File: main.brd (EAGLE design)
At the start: 50.8 x 50.8 mm, 54 parts, among them U2 SN65HVD32_D_8

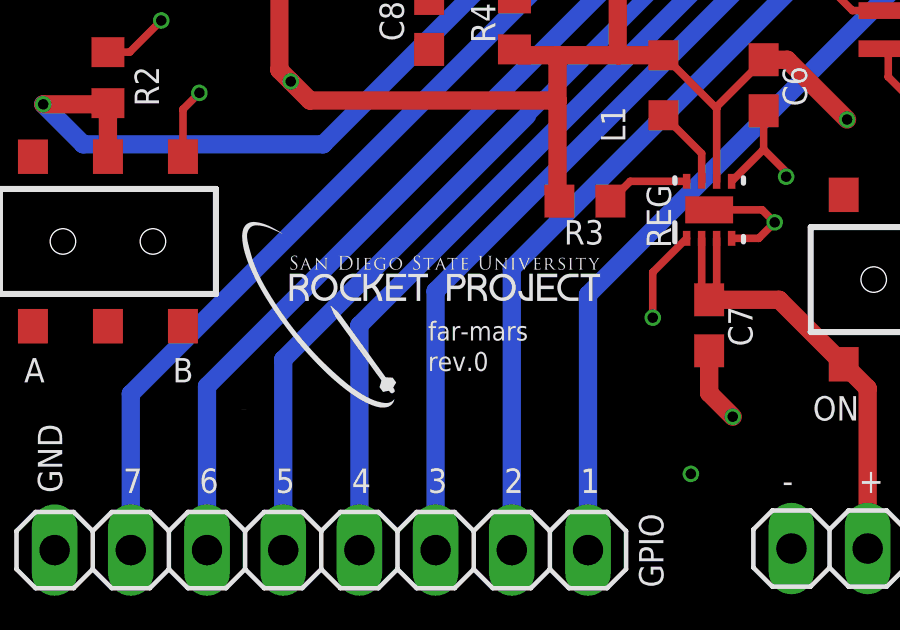
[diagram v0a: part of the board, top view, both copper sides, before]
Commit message: Some logo dpi fixes
OSHpark wouldn't except a silkscreen above 400 dpi
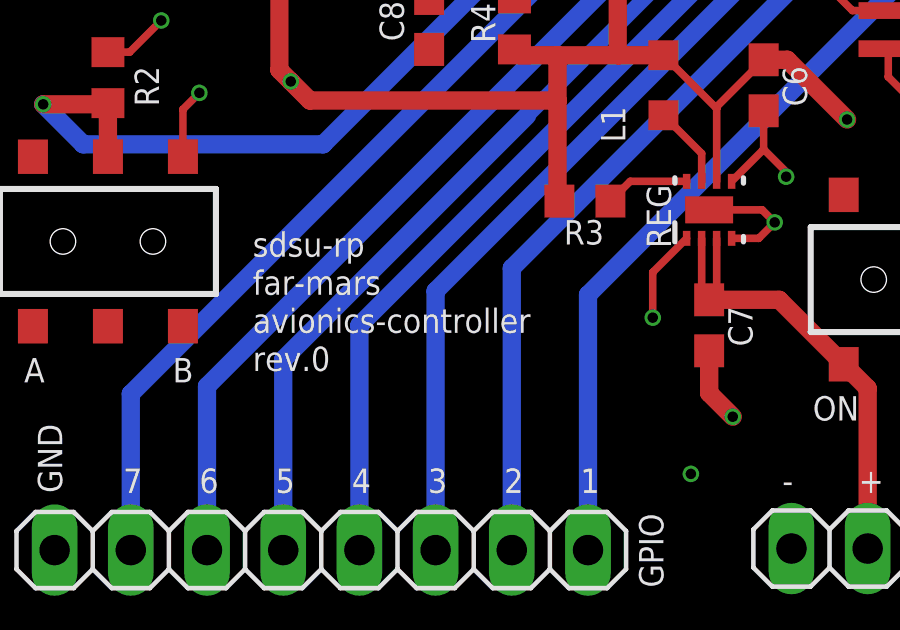
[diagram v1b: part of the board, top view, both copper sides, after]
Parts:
- removed U$6: (no value), cool:RP-LOGO-.15
- added U$5: (no value), cool:RP-LOGO-DPIFIX
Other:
- board text added: "avionics-controller"
- board text added: "sdsu-rp"
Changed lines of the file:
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@@
 <layers>
 <layer number="1" name="Top" color="4" fill="1" visible="yes" active="yes"/>
-<layer number="2" name="Route2" color="1" fill="3" visible="yes" active="yes"/>
+<layer number="2" name="Route2" color="1" fill="3" visible="no" active="yes"/>
 <layer number="3" name="Route3" color="4" fill="3" visible="no" active="no"/>
 <layer number="4" name="Route4" color="1" fill="4" visible="no" active="no"/>
@@
 <layer number="13" name="Route13" color="4" fill="5" visible="no" active="no"/>
 <layer number="14" name="Route14" color="1" fill="6" visible="no" active="no"/>
-<layer number="15" name="Route15" color="4" fill="6" visible="yes" active="yes"/>
-<layer number="16" name="Bottom" color="1" fill="1" visible="yes" active="yes"/>
+<layer number="15" name="Route15" color="4" fill="6" visible="no" active="yes"/>
+<layer number="16" name="Bottom" color="1" fill="1" visible="no" active="yes"/>
 <layer number="17" name="Pads" color="2" fill="1" visible="yes" active="yes"/>
 <layer number="18" name="Vias" color="2" fill="1" visible="yes" active="yes"/>
@@
 <text x="10.414" y="8.89" size="0.8128" layer="25">A</text>
 <text x="15.367" y="8.89" size="0.8128" layer="25">B</text>
-<text x="23.876" y="10.287" size="0.635" layer="21" font="vector">far-mars</text>
-<text x="23.876" y="9.271" size="0.635" layer="21" font="vector">rev.0</text>
+<text x="18.034" y="11.811" size="0.8128" layer="21" font="vector">far-mars</text>
+<text x="18.034" y="9.271" size="0.8128" layer="21" font="vector">rev.0</text>
+<text x="18.034" y="13.081" size="0.8128" layer="21" font="vector">sdsu-rp</text>
+<text x="18.034" y="10.541" size="0.8128" layer="21" font="vector">avionics-controller</text>
 </plain>
 <attributes>
@@
 <attribute name="VALUE" x="11.303" y="19.685" size="1.27" layer="27" rot="R270"/>
 </element>
-<element name="U$6" library="cool" package="RP-LOGO-.15" value="" x="17.653" y="8.001"/>
+<element name="U$5" library="cool" package="RP-LOGO-DPIFIX" value="" x="43.688" y="11.811" rot="MR0"/>
 </elements>
 <signals>

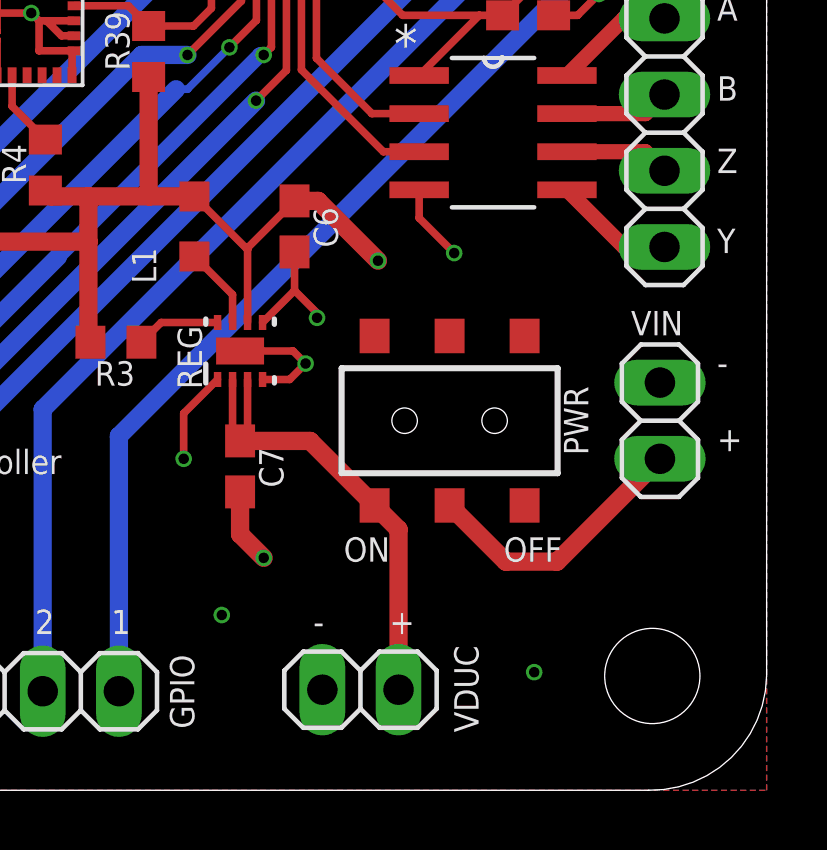
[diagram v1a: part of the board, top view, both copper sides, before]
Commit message: Small switch adjustment, and render update for this change
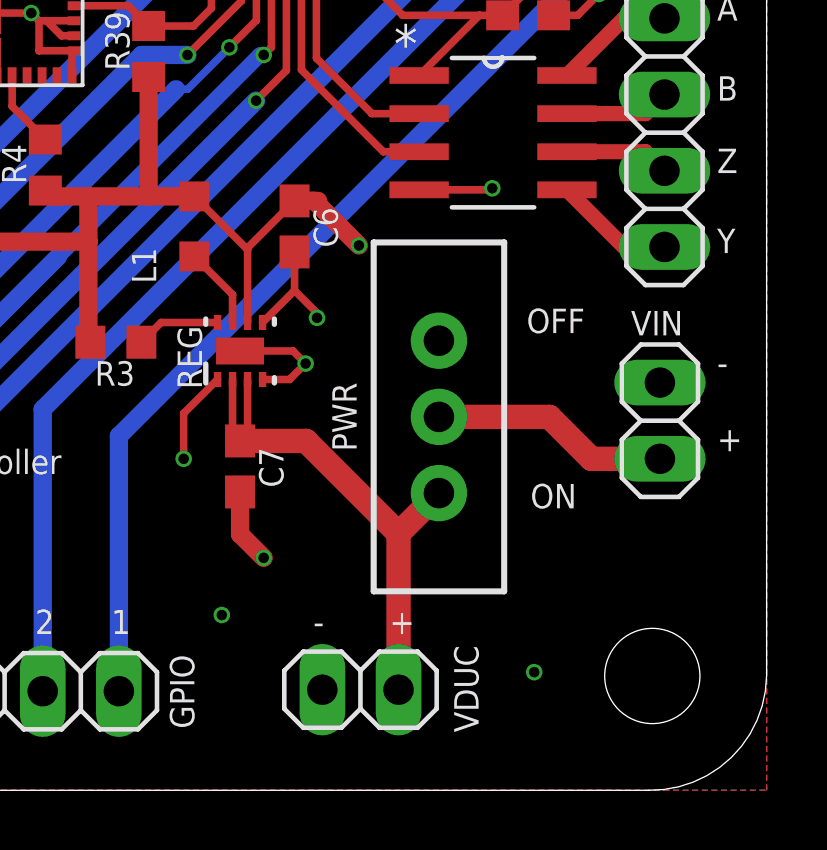
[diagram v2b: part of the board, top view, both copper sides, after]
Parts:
- PWR: device SparkFun-Switches:SWITCH_DPDT_SMD_AYZ0202 -> SparkFun-Switches:SWITCH_SPDT_PTH_11.6X4.0MM
- moved PWR 0.38 mm to (39.9, 12.4)
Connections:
- net VSYS: now also PWR.1; no longer PWR.3
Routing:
- net VSYS: track 16.2 -> 18.0 mm
- net N$9: track 9.21 -> 7.94 mm
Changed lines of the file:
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@@
 <text x="49.149" y="13.843" size="0.8128" layer="25">-</text>
 <text x="49.149" y="11.303" size="0.8128" layer="25">+</text>
-<text x="36.703" y="7.62" size="0.8128" layer="25">ON</text>
-<text x="42.037" y="7.62" size="0.8128" layer="25">OFF</text>
+<text x="42.926" y="9.398" size="0.8128" layer="25">ON</text>
+<text x="42.799" y="15.24" size="0.8128" layer="25">OFF</text>
 <text x="5.334" y="15.494" size="0.8128" layer="25">-</text>
 <text x="5.334" y="12.954" size="0.8128" layer="25">+</text>
@@
 <attribute name="VALUE" x="33.1597" y="19.431" size="1.27" layer="27" rot="R270"/>
 </element>
-<element name="PWR" library="SparkFun-Switches" package="SWITCH_DPDT_SMD_AYZ0202" value="" x="40.2336" y="12.319" smashed="yes" rot="R180">
-<attribute name="NAME" x="44.0436" y="12.319" size="0.8128" layer="25" ratio="20" rot="R270" align="bottom-center"/>
-<attribute name="PROD_ID" value="SWCH-08179" x="49.5808" y="25.1079" size="1.778" layer="27" rot="R180" display="off"/>
-<attribute name="SF_ID" value="COM-00597" x="49.5808" y="25.1079" size="1.778" layer="27" rot="R180" display="off"/>
-<attribute name="VALUE" x="36.4236" y="12.319" size="0.6096" layer="27" font="vector" ratio="20" rot="R270" align="top-center"/>
-</element>
 <element name="C7" library="resistor" package="C0603" value="10u" x="33.2486" y="10.795" smashed="yes" rot="R270">
 <attribute name="NAME" x="33.8836" y="11.43" size="0.8128" layer="25" rot="R270"/>
@@
 </element>
 <element name="U$5" library="cool" package="RP-LOGO-DPIFIX" value="" x="43.688" y="11.811" rot="MR0"/>
+<element name="PWR" library="SparkFun-Switches" package="SWITCH_SPDT_PTH_11.6X4.0MM" value="" x="39.878" y="12.446" smashed="yes" rot="R180">
+<attribute name="NAME" x="36.322" y="12.446" size="0.8128" layer="25" ratio="20" rot="R270" align="bottom-center"/>
+<attribute name="PROD_ID" value="SWCH-08261" x="39.878" y="12.446" size="1.778" layer="27" rot="R180" display="off"/>
+<attribute name="SF_SKU" value="COM-00102" x="39.878" y="12.446" size="1.778" layer="27" rot="R180" display="off"/>
+<attribute name="VALUE" x="37.465" y="12.446" size="0.6096" layer="27" font="vector" ratio="20" rot="R270" align="top-center"/>
+</element>
 </elements>
 <signals>
@@
 <wire x1="28.194" y1="14.9996" x2="28.2584" y2="14.9352" width="0.6096" layer="1"/>
 <wire x1="35.0647" y1="19.646" x2="35.853" y2="19.646" width="0.6096" layer="1"/>
-<wire x1="35.853" y1="19.646" x2="37.846" y2="17.653" width="0.6096" layer="1"/>
-<via x="37.846" y="17.653" extent="1-16" drill="0.35"/>
 <wire x1="28.194" y1="18.288" x2="19.939" y2="18.288" width="0.6096" layer="1"/>
 <wire x1="19.939" y1="18.288" x2="19.304" y2="18.923" width="0.6096" layer="1"/>
@@
 <via x="46.609" y="29.083" extent="1-16" drill="0.35"/>
 <wire x1="48.1457" y1="29.1093" x2="46.6353" y2="29.1093" width="0.254" layer="1"/>
+<wire x1="35.0647" y1="19.646" x2="35.726" y2="19.646" width="0.6096" layer="1"/>
+<wire x1="35.726" y1="19.646" x2="37.211" y2="18.161" width="0.6096" layer="1"/>
+<via x="37.211" y="18.161" extent="1-16" drill="0.35"/>
 </signal>
 <signal name="GND">
@@
 <wire x1="44.5008" y1="25.8318" x2="45.212" y2="26.543" width="0.254" layer="1"/>
 <via x="45.212" y="26.543" extent="1-16" drill="0.35"/>
-<wire x1="39.2176" y1="20.0152" x2="39.2176" y2="19.0754" width="0.254" layer="1"/>
-<wire x1="39.2176" y1="19.0754" x2="40.386" y2="17.907" width="0.254" layer="1"/>
-<via x="40.386" y="17.907" extent="1-16" drill="0.35"/>
 <wire x1="35.0647" y1="16.6592" x2="35.814" y2="15.9099" width="0.254" layer="1"/>
 <wire x1="35.814" y1="15.9099" x2="35.814" y2="15.748" width="0.254" layer="1"/>
@@
 <wire x1="25.15" y1="25.908" x2="26.289" y2="25.908" width="0.254" layer="1"/>
 <contactref element="GPIO" pad="8"/>
+<wire x1="39.2176" y1="20.0152" x2="41.6052" y2="20.0152" width="0.254" layer="1"/>
+<wire x1="41.6052" y1="20.0152" x2="41.656" y2="20.066" width="0.254" layer="1"/>
+<via x="41.656" y="20.066" extent="1-16" drill="0.35"/>
 </signal>
 <signal name="VDDCORE">
@@
 <contactref element="REG" pad="3"/>
 <contactref element="C7" pad="1"/>
-<contactref element="PWR" pad="3"/>
 <wire x1="33.2486" y1="11.645" x2="33.4986" y2="11.895" width="0.254" layer="1"/>
 <wire x1="33.4986" y1="11.895" x2="33.4986" y2="13.6931" width="0.254" layer="1"/>
 <wire x1="32.998596875" y1="13.6931" x2="32.998596875" y2="11.895003125" width="0.254" layer="1"/>
 <wire x1="32.998596875" y1="11.895003125" x2="33.2486" y2="11.645" width="0.254" layer="1"/>
-<wire x1="37.7336" y1="9.494" x2="35.5826" y2="11.645" width="0.6096" layer="1"/>
-<wire x1="35.5826" y1="11.645" x2="33.2486" y2="11.645" width="0.6096" layer="1"/>
-<wire x1="38.5318" y1="3.3528" x2="38.5318" y2="8.6958" width="0.6096" layer="1"/>
-<wire x1="38.5318" y1="8.6958" x2="37.7336" y2="9.494" width="0.6096" layer="1"/>
+<contactref element="PWR" pad="1"/>
+<wire x1="39.878" y1="9.906" x2="38.5318" y2="8.5598" width="0.8128" layer="1"/>
+<wire x1="38.5318" y1="8.5598" x2="38.5318" y2="3.3528" width="0.8128" layer="1"/>
+<wire x1="33.2486" y1="11.645" x2="35.4466" y2="11.645" width="0.8128" layer="1"/>
+<wire x1="35.4466" y1="11.645" x2="38.5318" y2="8.5598" width="0.8128" layer="1"/>
 </signal>
 <signal name="N$8">
@@
 </signal>
 <signal name="N$9">
+<contactref element="VIN" pad="2"/>
 <contactref element="PWR" pad="2"/>
-<contactref element="VIN" pad="2"/>
-<wire x1="40.2336" y1="9.494" x2="42.1076" y2="7.62" width="0.6096" layer="1"/>
-<wire x1="43.815" y1="7.62" x2="47.244" y2="11.049" width="0.6096" layer="1"/>
-<wire x1="42.1076" y1="7.62" x2="43.815" y2="7.62" width="0.6096" layer="1"/>
+<wire x1="47.244" y1="11.049" x2="44.958" y2="11.049" width="0.8128" layer="1"/>
+<wire x1="44.958" y1="11.049" x2="43.561" y2="12.446" width="0.8128" layer="1"/>
+<wire x1="43.561" y1="12.446" x2="39.878" y2="12.446" width="0.8128" layer="1"/>
 </signal>
 <signal name="GPIO1">

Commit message: Layout overview
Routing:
- net GND: track 84.7 -> 80.3 mm, vias 38 -> 41
- net VSYS: track 18.0 -> 16.7 mm
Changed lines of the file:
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@@
 <drawing>
 <settings>
-<setting alwaysvectorfont="yes"/>
+<setting alwaysvectorfont="no"/>
 <setting keepoldvectorfont="yes"/>
 <setting verticaltext="up"/>
@@
 <layer number="14" name="Route14" color="1" fill="6" visible="no" active="no"/>
 <layer number="15" name="Route15" color="4" fill="6" visible="no" active="yes"/>
-<layer number="16" name="Bottom" color="1" fill="1" visible="no" active="yes"/>
+<layer number="16" name="Bottom" color="1" fill="1" visible="yes" active="yes"/>
 <layer number="17" name="Pads" color="2" fill="1" visible="yes" active="yes"/>
 <layer number="18" name="Vias" color="2" fill="1" visible="yes" active="yes"/>
@@
 <wire x1="23.15" y1="23.8375" x2="23.15" y2="24.5875" width="0.254" layer="1"/>
 <wire x1="23.15" y1="24.5875" x2="23.0875" y2="24.65" width="0.254" layer="1"/>
-<wire x1="20.9305" y1="29.7688" x2="17.907" y2="29.7688" width="0.254" layer="1"/>
-<wire x1="17.907" y1="29.7688" x2="15.7774" y2="29.7688" width="0.254" layer="1"/>
-<wire x1="15.7774" y1="29.7688" x2="15.7218" y2="29.8244" width="0.254" layer="1"/>
-<wire x1="18.9366" y1="26.8605" x2="18.9366" y2="28.7392" width="0.254" layer="1"/>
-<wire x1="18.9366" y1="28.7392" x2="18.8214" y2="28.8544" width="0.254" layer="1"/>
-<wire x1="18.8214" y1="28.8544" x2="17.907" y2="29.7688" width="0.254" layer="1"/>
-<wire x1="18.8214" y1="28.8544" x2="18.0594" y2="28.8544" width="0.254" layer="1"/>
-<wire x1="18.0594" y1="28.8544" x2="17.399" y2="28.194" width="0.254" layer="1"/>
-<via x="17.399" y="28.194" extent="1-16" drill="0.35"/>
+<wire x1="15.7218" y1="29.8244" x2="15.7774" y2="29.7688" width="0.254" layer="1"/>
 <wire x1="2.9668" y1="35.2644" x2="1.5656" y2="35.2644" width="0.254" layer="1"/>
 <wire x1="1.5656" y1="35.2644" x2="1.524" y2="35.306" width="0.254" layer="1"/>
@@
 <wire x1="41.6052" y1="20.0152" x2="41.656" y2="20.066" width="0.254" layer="1"/>
 <via x="41.656" y="20.066" extent="1-16" drill="0.35"/>
+<wire x1="18.9366" y1="26.8605" x2="18.9366" y2="28.3074" width="0.4064" layer="1"/>
+<wire x1="18.9366" y1="28.3074" x2="18.923" y2="28.321" width="0.4064" layer="1"/>
+<via x="18.923" y="28.321" extent="1-16" drill="0.35"/>
+<wire x1="15.7774" y1="29.7688" x2="16.8148" y2="29.7688" width="0.4064" layer="1"/>
+<wire x1="16.8148" y1="29.7688" x2="16.891" y2="29.845" width="0.4064" layer="1"/>
+<via x="16.891" y="29.845" extent="1-16" drill="0.35"/>
+<wire x1="20.9305" y1="29.7688" x2="19.6088" y2="29.7688" width="0.4064" layer="1"/>
+<wire x1="19.6088" y1="29.7688" x2="19.558" y2="29.718" width="0.4064" layer="1"/>
+<via x="19.558" y="29.718" extent="1-16" drill="0.35"/>
+<wire x1="23.9141" y1="19.9907" x2="22.6813" y2="19.9907" width="0.4064" layer="1"/>
+<wire x1="22.6813" y1="19.9907" x2="22.105084375" y2="19.931915625" width="0.4064" layer="1"/>
+<via x="22.105084375" y="19.931915625" extent="1-16" drill="0.35"/>
+<wire x1="36.7792" y1="42.4688" x2="44.323" y2="44.069" width="0" layer="19" extent="1-1"/>
+<wire x1="36.195" y1="37.846" x2="36.7792" y2="41.1217" width="0" layer="19" extent="1-1"/>
+<wire x1="36.195" y1="46.609" x2="36.449" y2="42.799" width="0" layer="19" extent="1-1"/>
+<wire x1="32.004" y1="39.37" x2="35.294" y2="36.945" width="0" layer="19" extent="1-1"/>
+<wire x1="28.702" y1="38.735" x2="30.8102" y2="39.9678" width="0" layer="19" extent="1-1"/>
+<wire x1="25.908" y1="38.989" x2="28.2702" y2="39.1668" width="0" layer="19" extent="1-1"/>
+<wire x1="23.495" y1="38.735" x2="25.7302" y2="39.1668" width="0" layer="19" extent="1-1"/>
+<wire x1="20.6502" y1="39.9678" x2="23.1902" y2="39.9678" width="0" layer="19" extent="1-1"/>
+<wire x1="17.6406" y1="37.6044" x2="19.5952" y2="39.9678" width="0" layer="19" extent="1-1"/>
+<wire x1="35.56" y1="31.496" x2="35.294" y2="35.7079" width="0" layer="19" extent="1-1"/>
+<wire x1="35.56" y1="29.337" x2="35.8481" y2="31.2079" width="0" layer="19" extent="1-1"/>
+<wire x1="32.385" y1="30.607" x2="35.56" y2="31.496" width="0" layer="19" extent="1-1"/>
+<wire x1="40.513" y1="34.798" x2="38.794" y2="31.2079" width="0" layer="19" extent="1-1"/>
+<wire x1="17.653" y1="33.02" x2="18.034" y2="37.211" width="0" layer="19" extent="1-1"/>
+<wire x1="16.891" y1="29.845" x2="17.653" y2="33.02" width="0" layer="19" extent="1-1"/>
+<wire x1="18.923" y1="28.321" x2="16.8148" y2="29.7688" width="0" layer="19" extent="1-1"/>
+<wire x1="19.558" y1="29.718" x2="18.923" y2="28.321" width="0" layer="19" extent="1-1"/>
+<wire x1="23.0875" y1="26.15" x2="18.9366" y2="26.8605" width="0" layer="19" extent="1-1"/>
+<wire x1="22.105084375" y1="19.931915625" x2="23.15" y2="23.8375" width="0" layer="19" extent="1-1"/>
+<wire x1="14.9268" y1="25.5194" x2="18.9366" y2="26.8605" width="0" layer="19" extent="1-1"/>
+<wire x1="44.8174" y1="33.4899" x2="40.513" y2="34.798" width="0" layer="19" extent="1-1"/>
+<wire x1="46.8249" y1="35.3441" x2="46.8249" y2="32.8041" width="0" layer="19" extent="1-1"/>
+<wire x1="44.5126" y1="29.9094" x2="45.5032" y2="32.8041" width="0" layer="19" extent="1-1"/>
+<wire x1="45.212" y1="26.543" x2="45.339" y2="29.083" width="0" layer="19" extent="1-1"/>
+<wire x1="16.256" y1="18.542" x2="14.351" y2="23.368" width="0" layer="19" extent="1-1"/>
+<wire x1="9.2955" y1="22.225" x2="14.351" y2="23.368" width="0" layer="19" extent="1-1"/>
+<wire x1="4.572" y1="22.606" x2="9.2955" y2="22.225" width="0" layer="19" extent="1-1"/>
+<wire x1="4.445" y1="20.066" x2="4.572" y2="22.606" width="0" layer="19" extent="1-1"/>
+<wire x1="3.4671" y1="15.748" x2="4.445" y2="20.066" width="0" layer="19" extent="1-1"/>
+<wire x1="6.985" y1="14.478" x2="3.4671" y2="15.748" width="0" layer="19" extent="1-1"/>
+<wire x1="7.112" y1="9.398" x2="6.985" y2="14.478" width="0" layer="19" extent="1-1"/>
+<wire x1="3.302" y1="8.636" x2="7.112" y2="9.398" width="0" layer="19" extent="1-1"/>
+<wire x1="8.128" y1="5.334" x2="7.112" y2="9.398" width="0" layer="19" extent="1-1"/>
+<wire x1="11.43" y1="3.302" x2="8.128" y2="5.334" width="0" layer="19" extent="1-1"/>
+<wire x1="41.656" y1="20.066" x2="43.6998" y2="25.8318" width="0" layer="19" extent="1-1"/>
+<wire x1="35.0647" y1="17.946" x2="39.2176" y2="20.0152" width="0" layer="19" extent="1-1"/>
+<wire x1="33.248596875" y1="14.6431" x2="33.9986" y2="15.5931" width="0" layer="19" extent="1-1"/>
+<wire x1="32.4986" y1="13.6931" x2="33.248596875" y2="14.6431" width="0" layer="19" extent="1-1"/>
+<wire x1="33.2486" y1="9.945" x2="31.369" y2="11.049" width="0" layer="19" extent="1-1"/>
+<wire x1="32.639" y1="5.842" x2="34.036" y2="7.747" width="0" layer="19" extent="1-1"/>
+<wire x1="35.9918" y1="3.3528" x2="32.639" y2="5.842" width="0" layer="19" extent="1-1"/>
+<wire x1="43.053" y1="3.937" x2="35.9918" y2="3.3528" width="0" layer="19" extent="1-1"/>
+<wire x1="47.244" y1="13.589" x2="41.6052" y2="20.0152" width="0" layer="19" extent="1-1"/>
+<wire x1="2.9668" y1="35.2644" x2="3.5968" y2="25.4194" width="0" layer="19" extent="1-1"/>
+<wire x1="3.8518" y1="39.4044" x2="2.9668" y2="35.2644" width="0" layer="19" extent="1-1"/>
+<wire x1="10.033" y1="46.355" x2="5.5968" y2="39.4044" width="0" layer="19" extent="1-1"/>
 </signal>
 <signal name="VDDCORE">
@@
 <contactref element="C7" pad="1"/>
 <wire x1="33.2486" y1="11.645" x2="33.4986" y2="11.895" width="0.254" layer="1"/>
-<wire x1="33.4986" y1="11.895" x2="33.4986" y2="13.6931" width="0.254" layer="1"/>
 <wire x1="32.998596875" y1="13.6931" x2="32.998596875" y2="11.895003125" width="0.254" layer="1"/>
 <wire x1="32.998596875" y1="11.895003125" x2="33.2486" y2="11.645" width="0.254" layer="1"/>
@@
 <wire x1="33.2486" y1="11.645" x2="35.4466" y2="11.645" width="0.8128" layer="1"/>
 <wire x1="35.4466" y1="11.645" x2="38.5318" y2="8.5598" width="0.8128" layer="1"/>
+<wire x1="33.4986" y1="13.6931" x2="32.998596875" y2="13.6931" width="0.254" layer="1"/>
 </signal>
 <signal name="N$8">
